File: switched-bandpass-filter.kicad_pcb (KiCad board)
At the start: 2 copper layers, 82.1 x 72.6 mm, 69 parts, among them J1 SMA, J10 F3 out, J11 F4 out, J2 SMA, J3 F4 in, J5 F3 in, J6 F2 in, J7 F1 in, J8 F1 out, J9 F2 out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

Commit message: many of the FAB markings wanted to be silkscreen, and visaversa
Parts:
- renumbered 1 to J4
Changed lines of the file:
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@@
     (property "ki_keywords" "R res resistor")
     (attr smd)
-    (fp_text reference "R11" (at 0 -2.28) (layer "F.SilkS")
-        (effects (font (size 1 1) (thickness 0.15)))
-    )
-    (fp_text value "10K" (at 0 2.28) (layer "F.Fab")
+    (fp_text reference "R11" (at 0 -2.28) (layer "F.Fab") hide
+        (effects (font (size 1 1) (thickness 0.15)))
+    )
+    (fp_text value "10K" (at 0 2.28) (layer "F.SilkS")
         (effects (font (size 1 1) (thickness 0.15)))
     )
@@
     (property "ki_keywords" "connector")
     (attr through_hole)
-    (fp_text reference "1" (at 0 -2.33 180) (layer "F.SilkS") hide
+    (fp_text reference "J4" (at 0 -2.33 180) (layer "F.SilkS") hide
         (effects (font (size 1 1) (thickness 0.15)))
     )
@@
     (property "ki_keywords" "R res resistor")
     (attr smd)
-    (fp_text reference "R10" (at 0 -2.28) (layer "F.SilkS")
-        (effects (font (size 1 1) (thickness 0.15)))
-    )
-    (fp_text value "4.7K" (at 0 2.28) (layer "F.Fab")
+    (fp_text reference "R10" (at 0 -2.28) (layer "F.Fab") hide
+        (effects (font (size 1 1) (thickness 0.15)))
+    )
+    (fp_text value "4.7K" (at 0 2.28) (layer "F.SilkS")
         (effects (font (size 1 1) (thickness 0.15)))
     )
@@
         (effects (font (size 1 1) (thickness 0.15)))
     )
-    (fp_text value "1N4148" (at -0.04 2.32) (layer "F.SilkS")
+    (fp_text value "1N4148" (at 0.1046 -2.3596) (layer "F.SilkS")
         (effects (font (size 1 1) (thickness 0.15)))
     )
@@
     (property "ki_keywords" "diode")
     (attr smd)
-    (fp_text reference "D11" (at 0 -2.28) (layer "F.SilkS")
-        (effects (font (size 1 1) (thickness 0.15)))
-    )
-    (fp_text value "1N4148" (at 0 2.28) (layer "F.Fab")
+    (fp_text reference "D11" (at 0 -2.28) (layer "F.Fab") hide
+        (effects (font (size 1 1) (thickness 0.15)))
+    )
+    (fp_text value "1N4148" (at 0 2.28) (layer "F.SilkS")
         (effects (font (size 1 1) (thickness 0.15)))
     )
@@
     (property "ki_keywords" "diode")
     (attr smd)
-    (fp_text reference "D12" (at 0 -2.28) (layer "F.SilkS")
-        (effects (font (size 1 1) (thickness 0.15)))
-    )
-    (fp_text value "1N4148" (at 0 2.28) (layer "F.Fab")
+    (fp_text reference "D12" (at 0 -2.28) (layer "F.Fab") hide
+        (effects (font (size 1 1) (thickness 0.15)))
+    )
+    (fp_text value "1N4148" (at 0.2032 -2.3342) (layer "F.SilkS")
         (effects (font (size 1 1) (thickness 0.15)))
     )
@@
     (property "ki_keywords" "R res resistor")
     (attr smd)
-    (fp_text reference "R9" (at 0 -2.28) (layer "F.SilkS")
-        (effects (font (size 1 1) (thickness 0.15)))
-    )
-    (fp_text value "4.7K" (at 0 2.28) (layer "F.Fab")
+    (fp_text reference "R9" (at 0 -2.28) (layer "F.Fab") hide
+        (effects (font (size 1 1) (thickness 0.15)))
+    )
+    (fp_text value "4.7K" (at 0 2.28) (layer "F.SilkS")
         (effects (font (size 1 1) (thickness 0.15)))
     )
@@
     (property "ki_keywords" "cap capacitor")
     (attr smd)
-    (fp_text reference "C13" (at 0 -2.3) (layer "F.SilkS")
-        (effects (font (size 1 1) (thickness 0.15)))
-    )
-    (fp_text value "0.1 uF" (at 0 2.3) (layer "F.Fab")
+    (fp_text reference "C13" (at 0 -2.3) (layer "F.Fab") hide
+        (effects (font (size 1 1) (thickness 0.15)))
+    )
+    (fp_text value "0.1 uF" (at 0 2.3) (layer "F.SilkS")
         (effects (font (size 1 1) (thickness 0.15)))
     )
@@
     (property "ki_keywords" "NPN Transistor")
     (attr smd)
-    (fp_text reference "Q6" (at 0 -2.4) (layer "F.SilkS")
-        (effects (font (size 1 1) (thickness 0.15)))
-    )
-    (fp_text value "2N3904" (at 0 2.4) (layer "F.Fab")
+    (fp_text reference "Q6" (at 0 -2.4) (layer "F.Fab") hide
+        (effects (font (size 1 1) (thickness 0.15)))
+    )
+    (fp_text value "2N3904" (at 0 2.4) (layer "F.SilkS")
         (effects (font (size 1 1) (thickness 0.15)))
     )
@@
     (property "ki_keywords" "Voltage Regulator 100mA Positive")
     (attr smd)
-    (fp_text reference "U2" (at 0 -3.5) (layer "F.SilkS")
-        (effects (font (size 1 1) (thickness 0.15)))
-    )
-    (fp_text value "L78L05_SOT89" (at 0 3.5) (layer "F.Fab")
+    (fp_text reference "U2" (at 0 -3.5) (layer "F.Fab") hide
+        (effects (font (size 1 1) (thickness 0.15)))
+    )
+    (fp_text value "L78L05_SOT89" (at 0 3.5) (layer "F.SilkS")
         (effects (font (size 1 1) (thickness 0.15)))
     )
@@
     (property "ki_keywords" "R res resistor")
     (attr smd)
-    (fp_text reference "R12" (at 0 -2.28) (layer "F.SilkS")
-        (effects (font (size 1 1) (thickness 0.15)))
-    )
-    (fp_text value "10K" (at 0 2.28) (layer "F.Fab")
+    (fp_text reference "R12" (at 0 -2.28) (layer "F.Fab") hide
+        (effects (font (size 1 1) (thickness 0.15)))
+    )
+    (fp_text value "10K" (at 0 2.28) (layer "F.SilkS")
         (effects (font (size 1 1) (thickness 0.15)))
     )
@@
     (property "ki_keywords" "cap capacitor")
     (attr smd)
-    (fp_text reference "C14" (at 0 -2.3) (layer "F.SilkS")
-        (effects (font (size 1 1) (thickness 0.15)))
-    )
-    (fp_text value "10 uF" (at 0 2.3) (layer "F.Fab")
+    (fp_text reference "C14" (at 0 -2.3) (layer "F.Fab") hide
+        (effects (font (size 1 1) (thickness 0.15)))
+    )
+    (fp_text value "10 uF" (at 0 2.3) (layer "F.SilkS")
         (effects (font (size 1 1) (thickness 0.15)))
     )
@@
     (property "ki_keywords" "NPN Transistor")
     (attr smd)
-    (fp_text reference "Q5" (at 0 -2.4) (layer "F.SilkS")
-        (effects (font (size 1 1) (thickness 0.15)))
-    )
-    (fp_text value "2N3904" (at 0 2.4) (layer "F.Fab")
-        (effects (font (size 1 1) (thickness 0.15)))
-    )
+    (fp_text reference "Q5" (at 0 -2.4) (layer "F.Fab") hide
+        (effects (font (size 1 1) (thickness 0.15)))
+    )
+    (fp_text value "2N3904" (at 0 2.4) (layer "F.SilkS")
+        (effects (font (size 1 1) (thickness 0.15)))
+    )

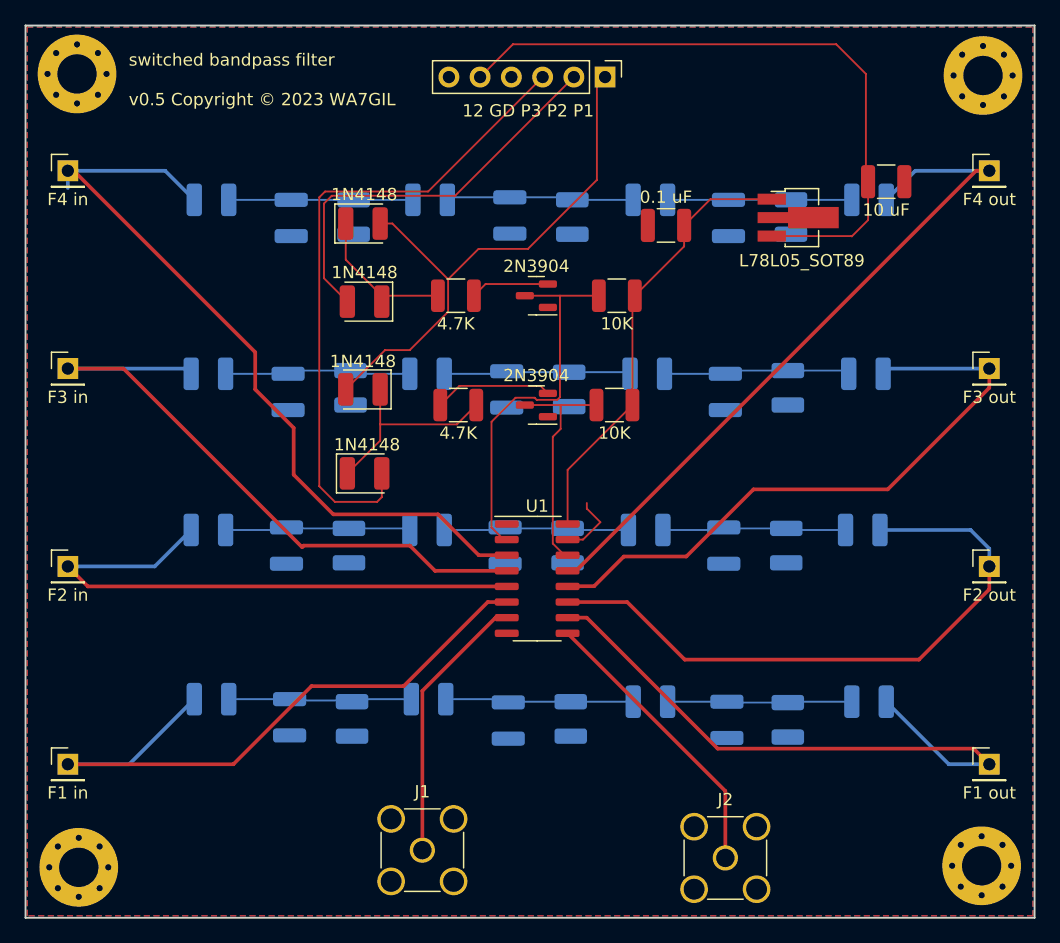
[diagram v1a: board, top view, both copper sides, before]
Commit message: v0.5 ATP; 3mm wide strips between filters; 3mm traces to SMA
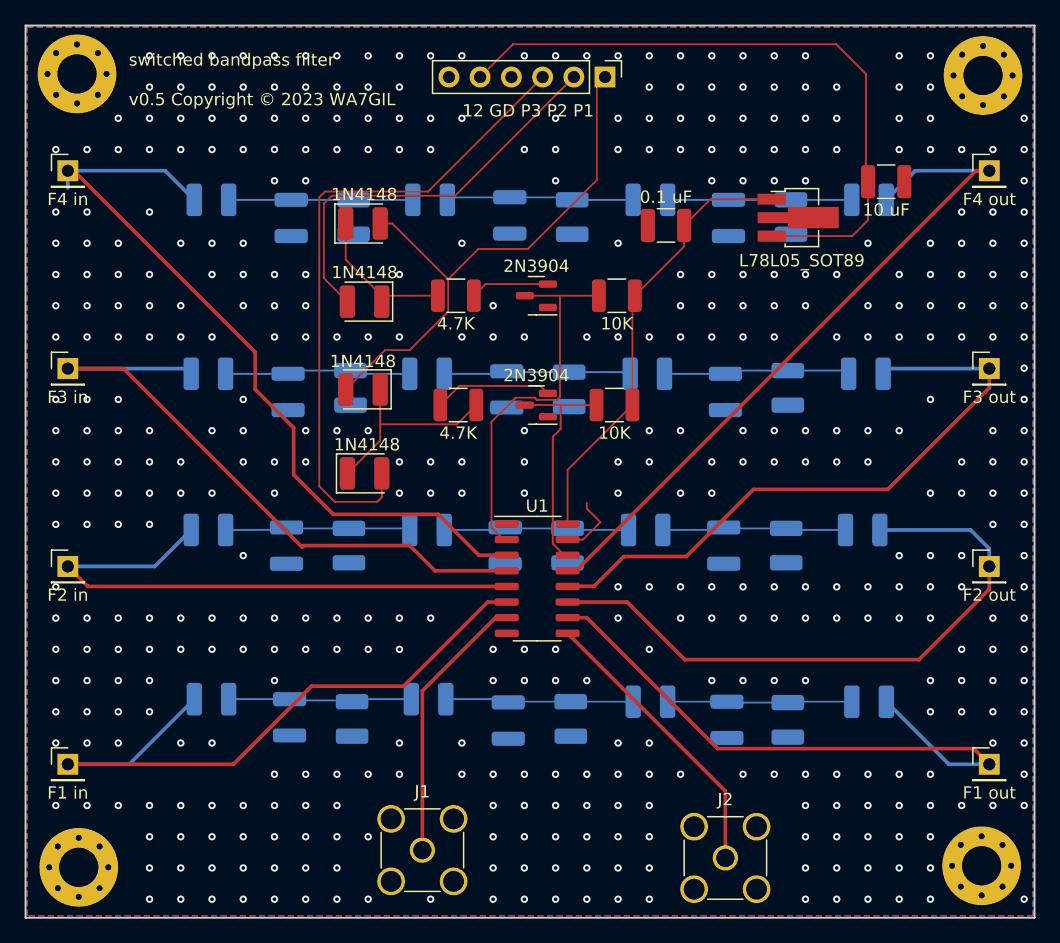
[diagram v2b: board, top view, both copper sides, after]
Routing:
- net GND: vias 0 -> 464

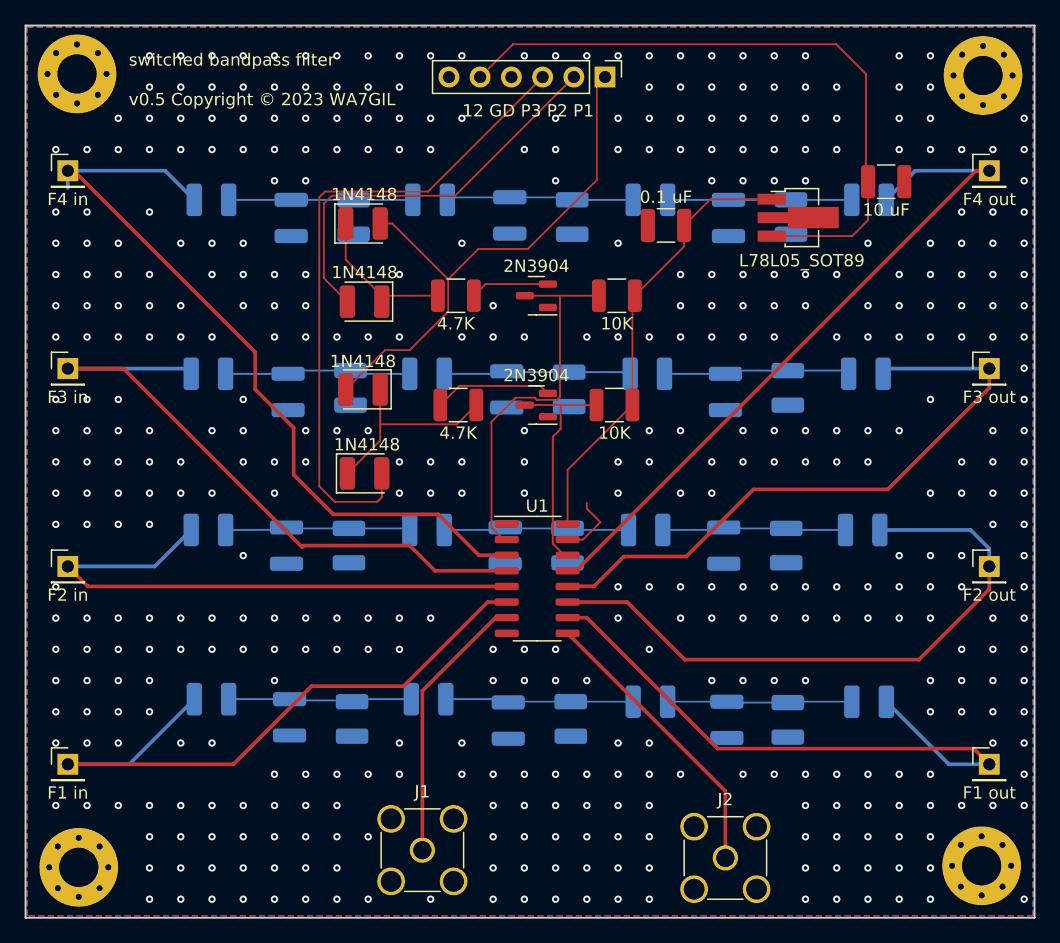
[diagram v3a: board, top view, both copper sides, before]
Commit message: v1.0 shipped to PCBWay
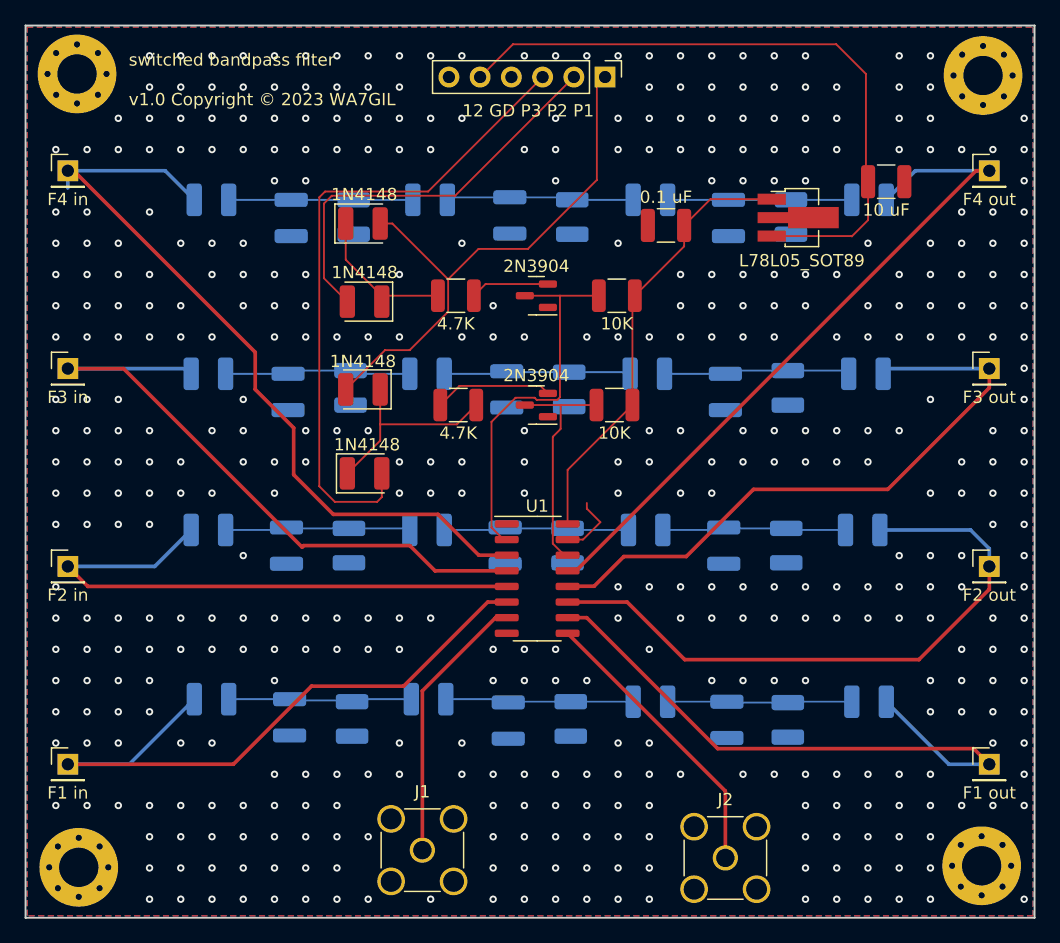
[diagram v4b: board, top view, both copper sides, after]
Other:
- rule pad_to_mask_clearance: 0.0508 -> 0
- board text added: "switched bandpass filter v1.0 Copyright © 2023 WA7GIL"
- board text removed: "switched bandpass filter v0.5 Copyright © 2023 WA7GIL"
